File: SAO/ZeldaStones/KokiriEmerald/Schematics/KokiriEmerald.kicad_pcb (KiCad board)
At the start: 2 copper layers, 60.8 x 73.2 mm, 34 parts, among them J1 Conn_02x03_Odd_Even

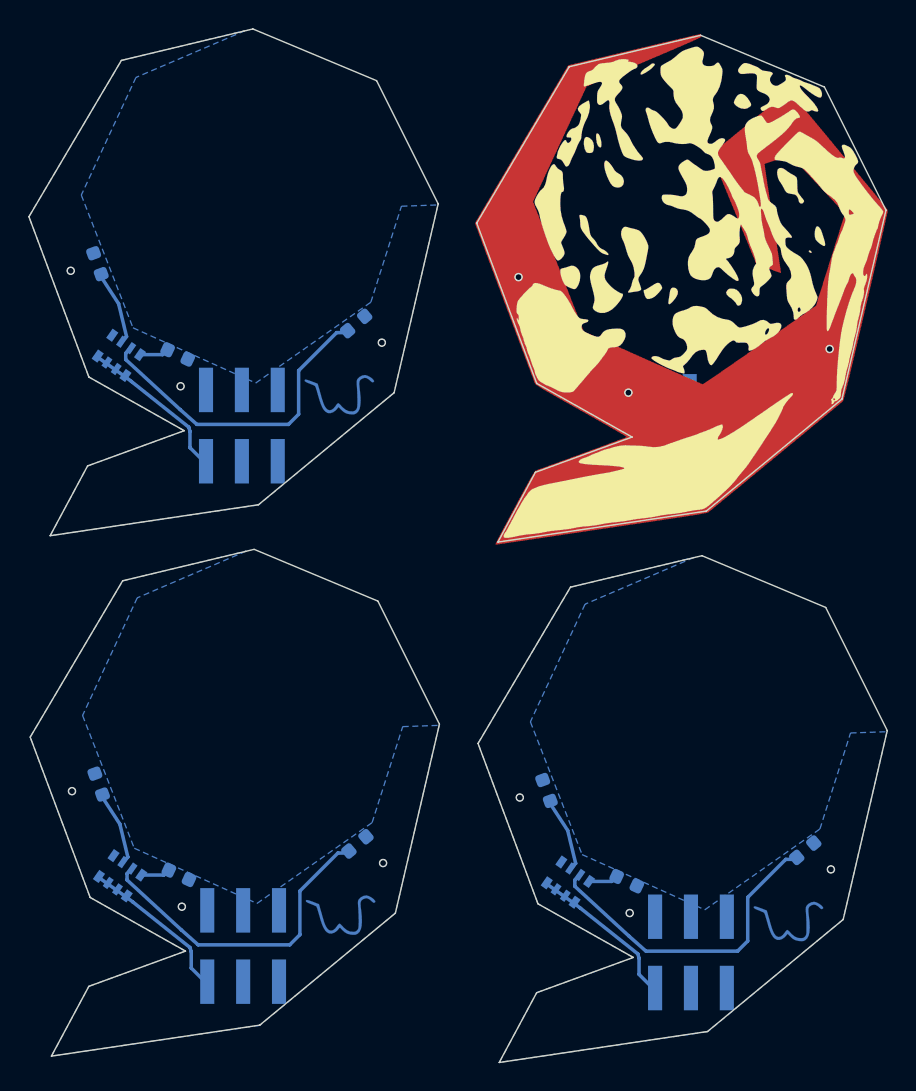
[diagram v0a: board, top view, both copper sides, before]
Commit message: Making stencils
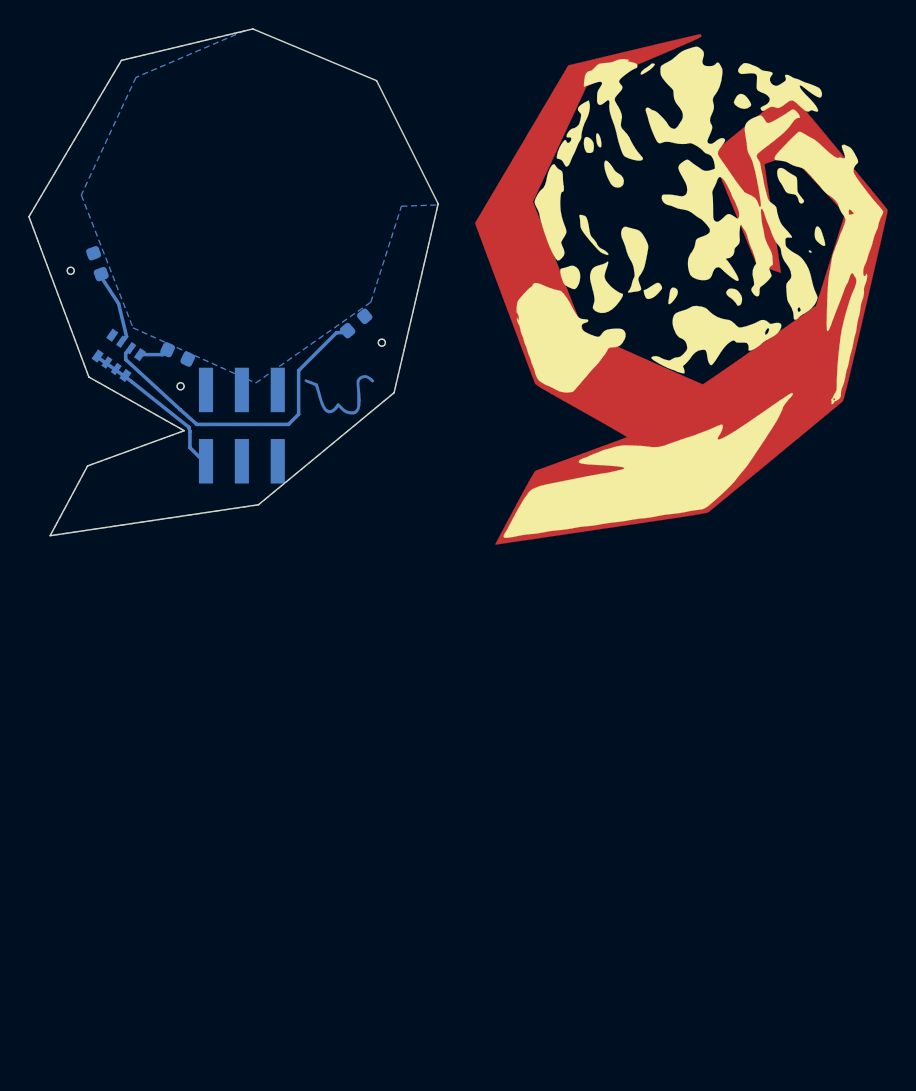
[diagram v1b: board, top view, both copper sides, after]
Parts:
- removed the D10 at (140.5, 135.9)
- removed the D10 at (108.7, 135.5)
- removed the D10 at (140.4, 99.1)
- removed the D12 at (103.1, 129.1)
- removed the D12 at (134.8, 129.5)
- removed the D12 at (134.7, 92.7)
- removed the D14 at (153.1, 133.7)
- removed the D14 at (121.4, 133.3)
- removed the D14 at (153.0, 96.9)
- removed the G*** at (112.2, 130.6) (x2)
- removed the G*** at (143.8, 94.2) (x4)
- removed the G*** at (143.9, 131.0) (x2)
- removed the J1 at (113.3, 140.5)
- removed the J1 at (145.0, 141.0)
- removed the J1 at (144.9, 104.1)
- removed the RN2 at (136.3, 136.0)
- removed the RN2 at (104.6, 135.6)
- removed the RN2 at (136.2, 99.2)
- removed the Ref** at (151.9, 139.8)
- removed the Ref** at (120.2, 139.4)
- removed the Ref** at (151.8, 103.0)
- added G*** (x2): LOGO, LOGO, F.Cu at (143.8, 94.2)
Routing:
- net Net-(D14-Pad1): track 91.2 -> 22.8 mm
- net VSS: track 44.7 -> 11.2 mm
- net Net-(D12-Pad1): track 21.4 -> 5.34 mm
- net Net-(RN2-Pad4): track 8.10 -> 2.03 mm
- net VCC: vias 12 -> 3
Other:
- board size 60.8 x 73.2 mm -> 29 x 35.9 mm
